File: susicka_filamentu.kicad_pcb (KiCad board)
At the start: 4 copper layers, 85 x 65 mm, 55 parts, among them J2 Conn_01x03, J3 Conn_01x04, J4 PJ-102AH, J5 Screw_Terminal_01x02, J6 Conn_01x04, J7 Conn_01x04, Q1 Q_NMOS_GSD, U1 RP2350A-QFN60, U2 RM2, U3 W25Q128JVS, U4 AP63203WU, Y1 Crystal_GND24

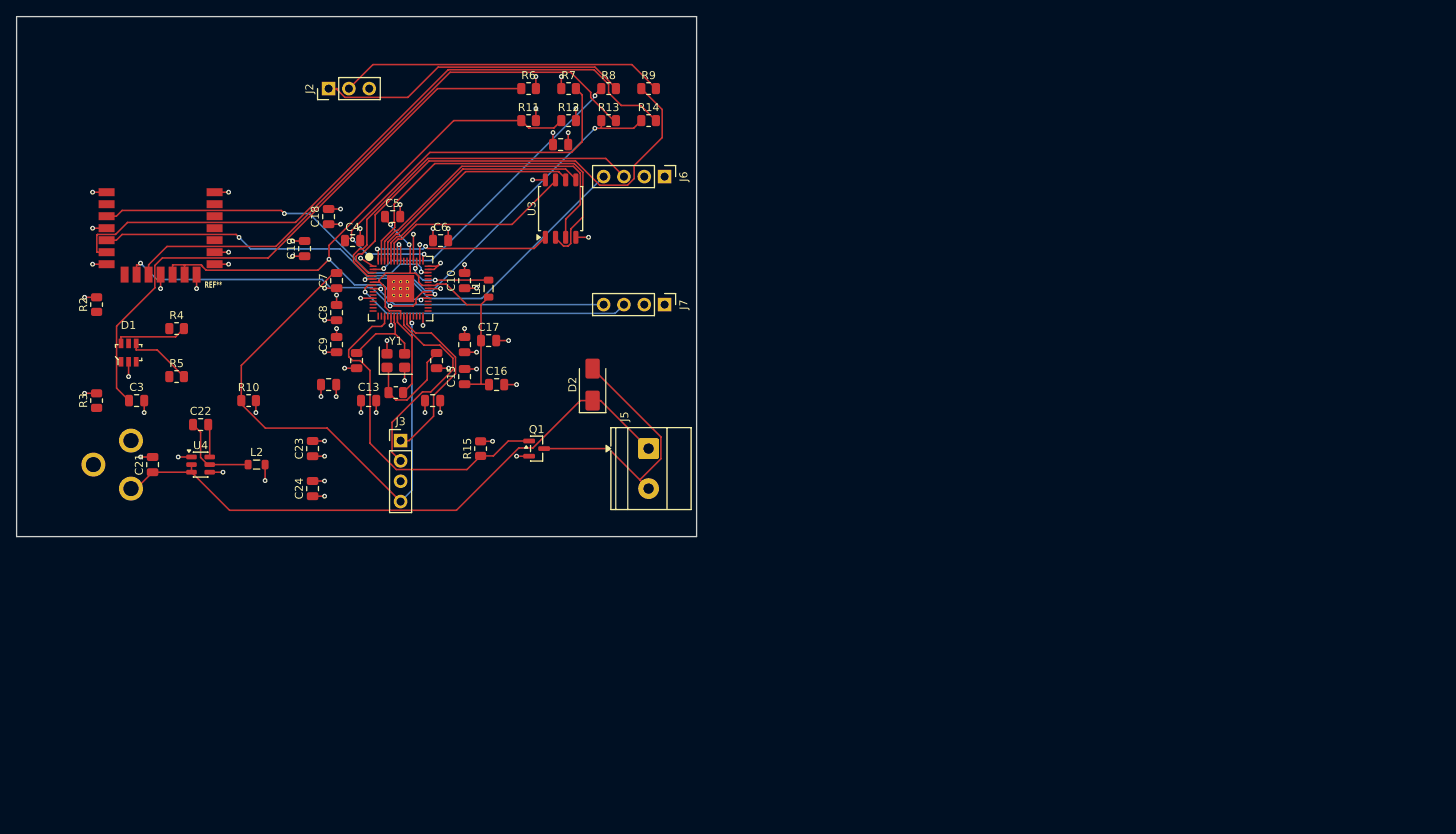
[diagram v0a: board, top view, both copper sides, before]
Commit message: Replace Gemini-generated layout with clean project for manual layout
Remove generated scripts, test boards, DRC reports, renders and build
output; restore the sandbox project so the PCB layout can be done by hand.

Co-Authored-By: Claude Opus 5.5 <noreply@anthropic.com>
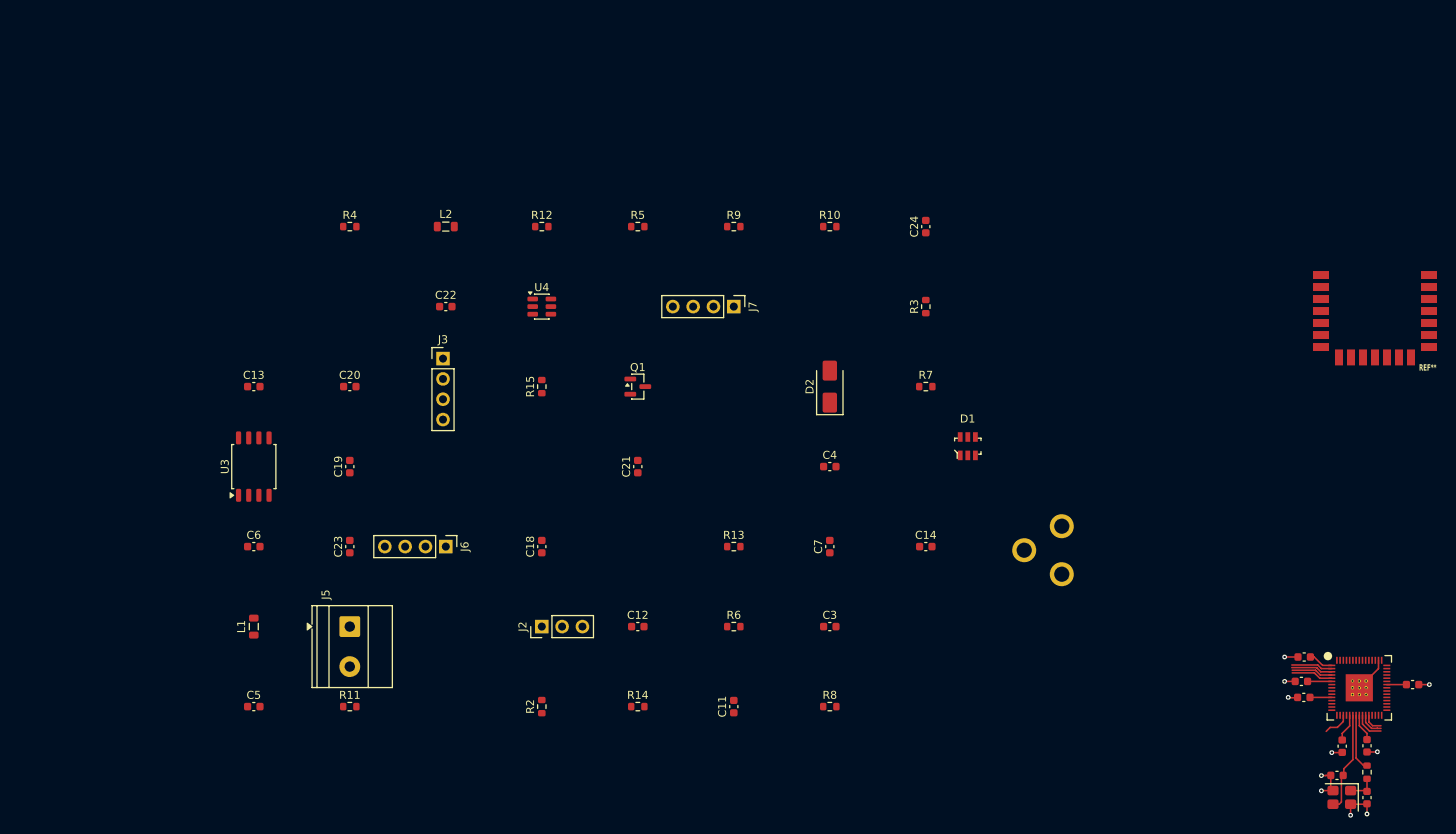
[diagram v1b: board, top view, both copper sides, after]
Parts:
- C1, C10, C11, C12, C13, C14, C15, C16, C17, C18, C19, C2, C20, C21, C22, C23, C24, C3, C4, C5, C6, C7, C8, C9: footprint Capacitor_SMD:C_0805_2012Metric -> Capacitor_SMD:C_0603_1608Metric
- R1, R10, R11, R12, R13, R14, R15, R2, R3, R4, R5, R6, R7, R8, R9: footprint Resistor_SMD:R_0805_2012Metric -> Resistor_SMD:R_0603_1608Metric
- moved U2 152.2 mm to (169.8, 34.9)
- moved C8 136.9 mm to (165.7, 91.2), turned to -90 degrees
- moved C1 133.1 mm to (165.1, 94.8), turned to 0 degrees
- moved R1 130.3 mm to (168.8, 94.5), turned to 90 degrees
- moved Y1 130.2 mm to (165.7, 97.6), turned to 180 degrees
- moved U1 129.8 mm to (167.8, 83.9)
- moved C9 128.7 mm to (160.9, 85.1), turned to 180 degrees
- moved C2 128.5 mm to (168.8, 97.6)
- moved C15 124.6 mm to (174.5, 83.5), turned to 0 degrees
- moved C17 120.9 mm to (168.8, 91.2), turned to -90 degrees
- moved J4 116.8 mm to (126.3, 66.7)
- moved C10 115.0 mm to (160.9, 80.0), turned to 180 degrees
- moved C16 107.2 mm to (160.6, 83.1), turned to 180 degrees
- moved D1 105.6 mm to (118.9, 53.7)
- moved R3 104.3 mm to (113.7, 36.2)
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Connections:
- D2 pad 1: 24V -> (no net)
- D2 pad 2: Net-(J5-Pin_2) -> (no net)
- J7 pad 1: GND -> +3V3
- J7 pad 2: unconnected-(J7-Pin_2-Pad2) -> GND
- U2 pad 20: (no net) -> unconnected-(U2-NC-Pad20)
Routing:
- net Net-(U2-DO): track 85.1 -> 0.00 mm
- net /RM2/RM2_DI: track 81.3 -> 0.00 mm, vias 3 -> 0
- net 24V: track 76.6 -> 0.00 mm
- net /RM2/RM2_BT_ON: track 75.8 -> 0.00 mm, vias 2 -> 0
- net Net-(J1-SHIELD): track 74.5 -> 0.00 mm
- net Net-(U2-nIRQ): track 72.5 -> 0.00 mm
- net Net-(J3-Pin_4): track 70.3 -> 2.54 mm, vias 1 -> 0
- net Net-(U1-GPIO1): track 60.3 -> 5.22 mm
- net Net-(U1-VREG_AVDD): track 53.1 -> 0.00 mm, vias 2 -> 0
- net /flash/QSPI_SD1: track 46.1 -> 0.00 mm
- net /RM2/RM2_SCLK: track 44.9 -> 0.00 mm, vias 2 -> 0
- net GND: track 64.5 -> 22.6 mm, vias 42 -> 10
- net /RM2/RM2_CS: track 41.0 -> 0.00 mm, vias 2 -> 0
- net Net-(J2-Pin_2): track 40.9 -> 0.00 mm
- net +3V3: track 49.8 -> 9.31 mm, vias 28 -> 0
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- removed copper zone on In2.Cu, net +3V3
- removed copper zone on In1.Cu, net GND
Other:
- board outline removed

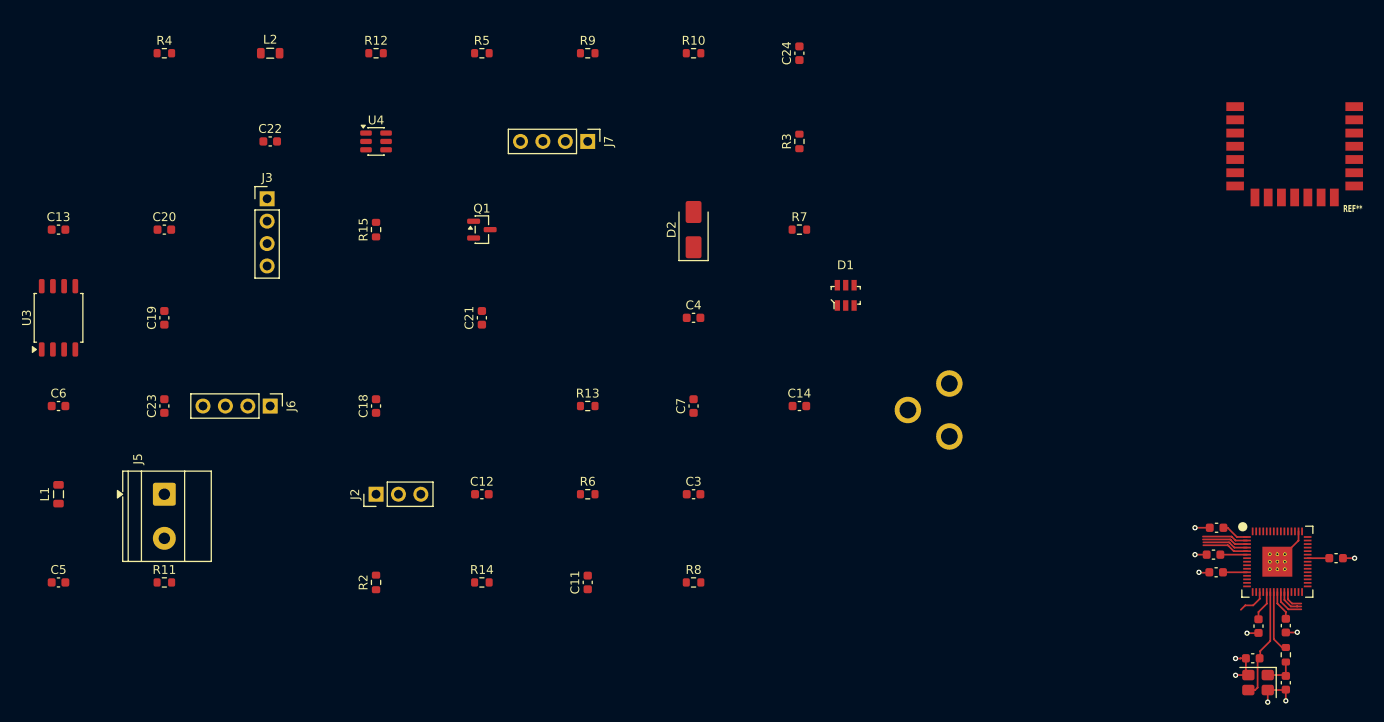
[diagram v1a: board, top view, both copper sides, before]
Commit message: Complete schematic for first prototype
- Footprints: passives 0402/0603 (larger only for 24 V / DC bias),
  U1 and L1 footprints taken from RP2350A Minimal R4 reference (MIT)
- New sheet vystupy: heater (Q1 SiS434DN) with thermal fuse terminal J13,
  fan (GPIO13) and exhaust fan (GPIO12) with AO3422, input protection
  (fuse, AOD4185 reverse polarity, SMBJ24CA TVS, bulk cap), status LED on
  RM2 GPIO0, button GPIO15, NTC on ADC0 (22k pull-up), I2C1 pull-ups,
  second SHT40 on I2C0 (GPIO8/9)
- New sheet rozsireni: spare GPIO header J12, test points TP1-TP5,
  mounting holes H1-H4
- Selected parts with Manufacturer/MPN fields; L2 4.7 uH Wurth 74438356047
- Fix D2 pin mapping (Device:D_Schottky), remove duplicate pull-down R12,
  C16 changed to 100 nF for third DVDD pin, Y1 value set
- Project footprint library susicka.pretty (PowerPAK 1212-8 with G/S/D pads)

Co-Authored-By: Claude Opus 5.5 <noreply@anthropic.com>
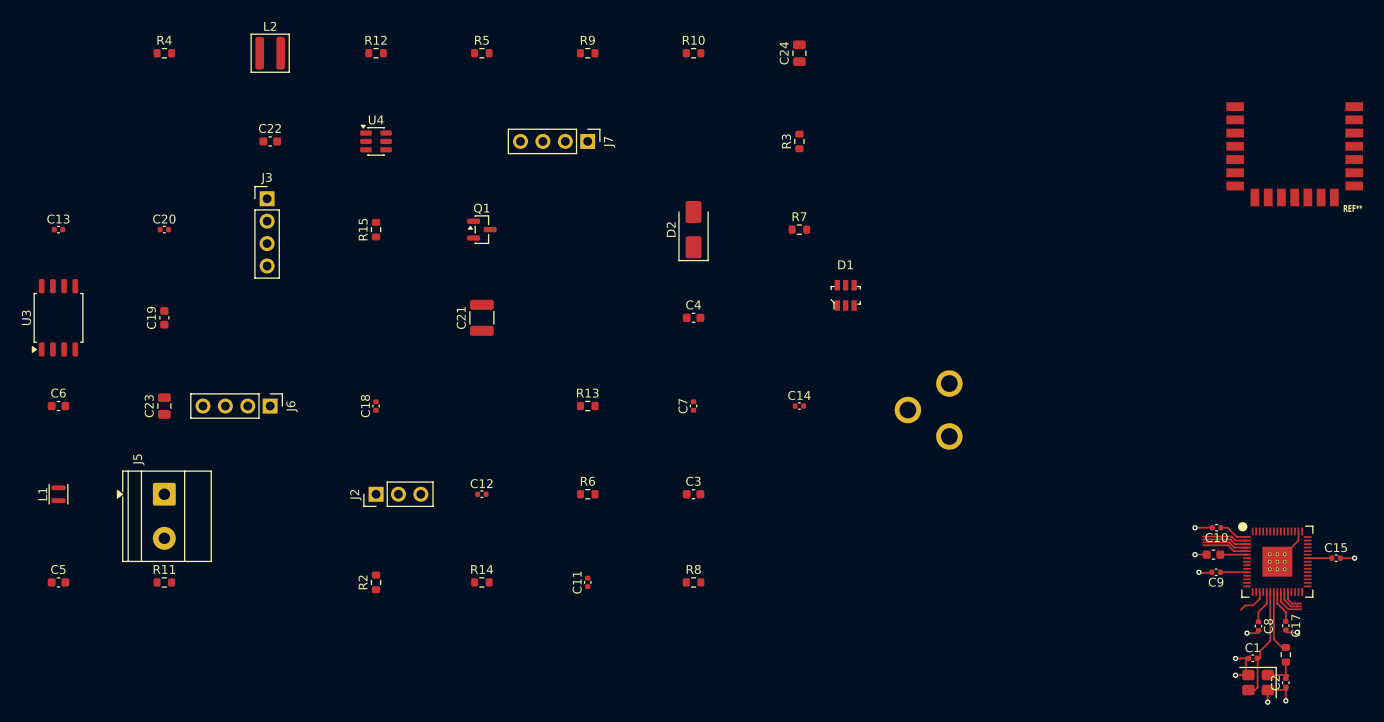
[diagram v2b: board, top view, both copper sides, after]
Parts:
- C1, C10, C11, C12, C13, C14, C15, C17, C18, C2, C20, C7, C8, C9: footprint Capacitor_SMD:C_0603_1608Metric -> Capacitor_SMD:C_0402_1005Metric
- C21: footprint Capacitor_SMD:C_0603_1608Metric -> Capacitor_SMD:C_1210_3225Metric
- C23, C24: footprint Capacitor_SMD:C_0603_1608Metric -> Capacitor_SMD:C_0805_2012Metric
- L1: footprint Inductor_SMD:L_0805_2012Metric -> Inductor_SMD:L_Murata_DFE201610P
- L2: footprint Inductor_SMD:L_0805_2012Metric -> Inductor_SMD:L_Wuerth_MAPI-4020
